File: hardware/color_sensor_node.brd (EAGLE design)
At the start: 27.9 x 27.9 mm, 20 parts, among them Q1 20V/4.2A/52mΩ/1.4W, U1 ISL29125, U2 3.3V, U3 WS2811

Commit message: Update color_sensor_node.brd
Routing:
- net 5V: track 49.7 -> 48.9 mm
- net GND: vias 23 -> 22

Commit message: add version number
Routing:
- net SCL: track 28.6 -> 28.1 mm
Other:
- board text added: "v01"
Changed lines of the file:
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@@
 <vertex x="5.08" y="15.24"/>
 </polygon>
+<text x="0.381" y="8.382" size="1.778" layer="1" font="vector" ratio="15" rot="SR270">v01</text>
 </plain>
 <attributes>
@@
 <wire x1="14.69" y1="14.47" x2="15.24" y2="14.47" width="0.2032" layer="1"/>
 <wire x1="16.51" y1="7.62" x2="21.59" y2="2.54" width="0.2032" layer="1"/>
-<wire x1="21.59" y1="4.445" x2="21.59" y2="2.54" width="0.4064" layer="16"/>
-<wire x1="21.59" y1="4.445" x2="20.828" y2="5.207" width="0.4064" layer="16"/>
-<wire x1="20.828" y1="5.207" x2="14.097" y2="5.207" width="0.4064" layer="16"/>
+<wire x1="21.59" y1="3.556" x2="21.59" y2="2.54" width="0.4064" layer="16"/>
+<wire x1="21.59" y1="3.556" x2="19.939" y2="5.207" width="0.4064" layer="16"/>
+<wire x1="19.939" y1="5.207" x2="14.097" y2="5.207" width="0.4064" layer="16"/>
 <wire x1="14.097" y1="5.207" x2="11.43" y2="2.54" width="0.4064" layer="16"/>
 <wire x1="15.24" y1="14.47" x2="16.51" y2="13.2" width="0.2032" layer="1"/>
@@
 <mfgpreviewcolor name="substratecolor" color="0xFF786E46"/>
 </mfgpreviewcolors>
-<errors>
-</errors>
 </board>
 </drawing>

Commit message: update packages, add rc filter to sensor vdd, move to smd connectors
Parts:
- removed J3: (no value), SparkFun-Connectors:2X5_PTH_SILK_.05
- added C3: 0.1uF, SparkFun-Capacitors:0603
- added J1: JTAG, SparkFun-Connectors:2X5-SMD-1.27MM
- added R3: 330, SparkFun-Resistors:0603
- D1: value WS2812-2020 -> WS2812B; device SparkFun-LED:WS2812-2020 -> SparkFun-LED:WS2812B
- J2: value (none) -> JTAG; device SparkFun-Connectors:2X5_PTH_SILK_.05 -> SparkFun-Connectors:2X5-SMD-1.27MM
- U3: device ws2811:MSOP8 -> ws2811:SOIC-8
- moved J2 12.8 mm to (19.1, 2.54)
- moved U1 5.08 mm to (19.1, 14.0)
- moved R1 3.54 mm to (17.8, 19.1), turned to 270 degrees
- moved D1 2.54 mm to (14.0, 14.0), turned to 180 degrees
- moved C1 1.27 mm to (8.13, 19.1)
- moved C2 1.27 mm to (2.54, 19.1)
- moved Q1 1.27 mm to (12.1, 19.1)
- moved R2 1.27 mm to (9.65, 19.1)
- moved U2 1.27 mm to (5.33, 19.1)
- moved U3 0.38 mm to (5.08, 14.0)
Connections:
- new net N$5: Q1.3, R3.2
- net 5V: now also D1.1, J1.4, J1.5, J1.7, J1.9; no longer D1.4, J3.4, J3.5, J3.7, J3.9
- net DIN: now also J1.6; no longer J2.6
- net DOUT: now also D1.2, J2.6; no longer D1.1, J3.6
- net GND: now also C3.2, D1.3, J1.1, J1.2, J1.3; no longer D1.2, J3.1, J3.2, J3.3
- net N$2: now also C3.1, R3.1; no longer Q1.3
- net N$4: now also D1.4; no longer D1.3
- net SCL: now also J1.10; no longer J3.10
- net SDA: now also J1.8; no longer J3.8
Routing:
- net 5V: track 48.9 -> 60.2 mm, vias 1 -> 0
- net GND: track 5.48 -> 16.5 mm, vias 22 -> 27
- net SCL: track 28.1 -> 36.5 mm
- net N$4: track 6.18 -> 10.7 mm
- net N$1: track 3.64 -> 7.65 mm
- net DIN: track 13.5 -> 16.2 mm
- net N$5: track 0.00 -> 2.43 mm
- net N$2: track 5.39 -> 7.02 mm
- net N$3: track 13.2 -> 14.1 mm
- net SDA: track 27.4 -> 26.6 mm, vias 2 -> 1

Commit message: Update color_sensor_node.brd
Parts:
- moved J1 12.5 mm to (3.81, 14.0), flipped to the bottom, turned to 90 degrees
- moved J2 12.5 mm to (24.1, 14.0), flipped to the bottom, turned to 90 degrees
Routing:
- net 5V: track 60.2 -> 28.5 mm, vias 0 -> 1
- net SCL: track 36.5 -> 11.1 mm, vias 0 -> 1
- net SDA: track 26.6 -> 8.64 mm
- net DOUT: track 14.3 -> 1.54 mm, vias 0 -> 1
- net DIN: track 16.2 -> 11.7 mm, vias 0 -> 1
- net GND: vias 27 -> 23

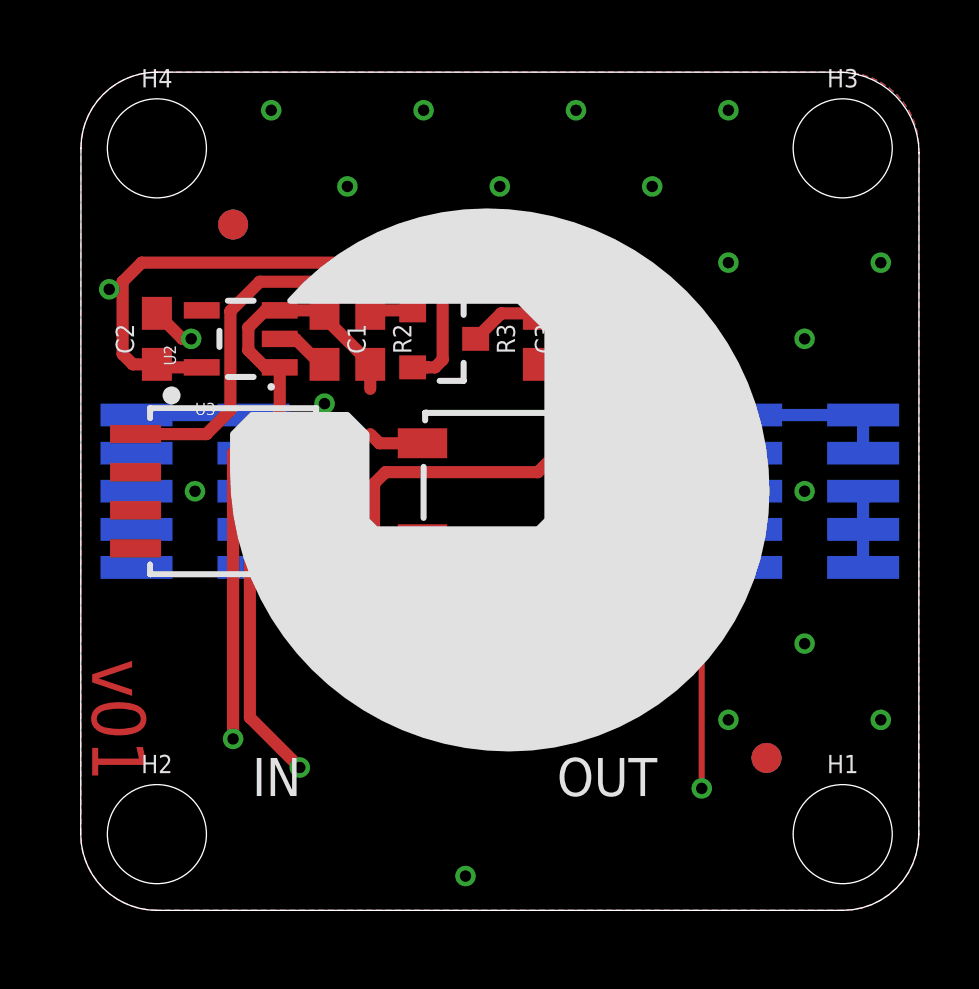
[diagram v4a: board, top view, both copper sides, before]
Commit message: simplify, remove mosfet
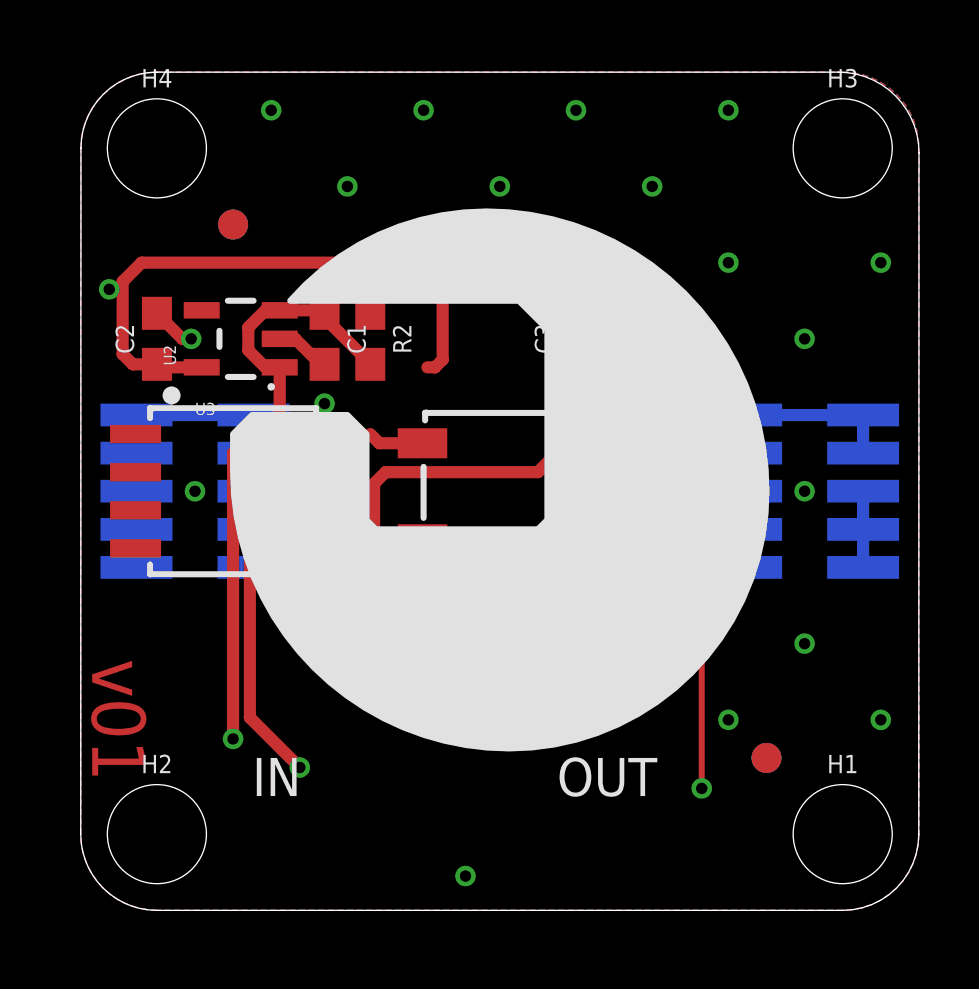
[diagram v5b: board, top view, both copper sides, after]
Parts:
- removed Q1: 20V/4.2A/52mΩ/1.4W, SparkFun-DiscreteSemi:SOT23-3
- removed R3: 330, SparkFun-Resistors:0603
- C3: value 0.1uF -> 1.0uF
- R2: value 287 -> 220
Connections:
- removed net N$3: Q1.1, R2.1, U3.1
- removed net N$5: Q1.3, R3.2
- net 3.3V: now also R2.2; no longer Q1.2
- net 5V: no longer R2.2
- net N$2: now also R2.1, U3.1; no longer R3.1
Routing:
- net N$3: track 14.1 -> 0.00 mm
- net N$5: track 2.43 -> 0.00 mm
- net N$2: track 7.02 -> 5.75 mm
- net 5V: track 28.5 -> 27.7 mm
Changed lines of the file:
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@@
 <attribute name="REV" value="" x="74.93" y="-20.32" size="1.778" layer="27" display="off"/>
-</element>
-<element name="Q1" library="SparkFun-DiscreteSemi" package="SOT23-3" value="20V/4.2A/52mΩ/1.4W" x="12.065" y="19.05" rot="R270">
-<attribute name="NAME" x="12.065" y="20.701" size="0.6096" layer="25" font="vector" ratio="20" align="bottom-center"/>
-<attribute name="PROD_ID" value="TRAN-14388" x="6.985" y="3.81" size="1.778" layer="27" rot="R270" display="off"/>
-<attribute name="VALUE" x="12.065" y="17.399" size="0.6096" layer="27" font="vector" ratio="20" align="top-center"/>
 </element>
 <element name="R1" library="SparkFun-Resistors" package="0603" value="10k" x="17.78" y="19.05" rot="R270">
@@
 <attribute name="VALUE" x="17.018" y="19.05" size="0.6096" layer="27" font="vector" ratio="20" rot="R270" align="top-center"/>
 </element>
-<element name="R2" library="SparkFun-Resistors" package="0603" value="287" x="9.652" y="19.05" rot="R270">
+<element name="R2" library="SparkFun-Resistors" package="0603" value="220" x="9.652" y="19.05" rot="R270">
 <attribute name="NAME" x="10.414" y="19.05" size="0.6096" layer="25" font="vector" ratio="20" rot="R270" align="bottom-center"/>
-<attribute name="PROD_ID" value="RES-10752" x="-18.288" y="-7.62" size="1.778" layer="27" rot="R270" display="off"/>
-<attribute name="VALUE" x="8.89" y="19.05" size="0.6096" layer="27" font="vector" ratio="20" rot="R270" align="top-center"/>
+<attribute name="PROD_ID" value="RES-07861" x="-18.288" y="-7.62" size="1.778" layer="27" rot="R270" display="off"/>
+<attribute name="VALUE" value="220" x="8.89" y="19.05" size="0.6096" layer="27" font="vector" ratio="20" rot="R270" align="top-center"/>
 </element>
 <element name="U1" library="SparkFun-Sensors" package="ODFN-6" value="ISL29125" x="19.05" y="13.97">
@@
 <attribute name="VALUE" value="JTAG" x="21.6662" y="12.1412" size="0.6096" layer="28" font="vector" ratio="20" rot="MR90"/>
 </element>
-<element name="C3" library="SparkFun-Capacitors" package="0603" value="0.1uF" x="16.51" y="19.05" rot="R90">
+<element name="C3" library="SparkFun-Capacitors" package="0603" value="1.0uF" x="16.51" y="19.05" rot="R90">
 <attribute name="NAME" x="15.748" y="19.05" size="0.6096" layer="25" font="vector" ratio="20" rot="R90" align="bottom-center"/>
-<attribute name="PROD_ID" value="CAP-00810" x="16.51" y="19.05" size="1.778" layer="27" font="vector" ratio="15" rot="R90" display="off"/>
-<attribute name="VALUE" value="0.1uF" x="17.272" y="19.05" size="0.6096" layer="27" font="vector" ratio="20" rot="R90" align="top-center"/>
-</element>
-<element name="R3" library="SparkFun-Resistors" package="0603" value="330" x="15.24" y="19.05" rot="R90">
-<attribute name="NAME" x="14.478" y="19.05" size="0.6096" layer="25" font="vector" ratio="20" rot="R90" align="bottom-center"/>
-<attribute name="PROD_ID" value="RES-00818" x="15.24" y="19.05" size="1.778" layer="27" font="vector" ratio="15" rot="R90" display="off"/>
-<attribute name="VALUE" value="330" x="16.002" y="19.05" size="0.6096" layer="27" font="vector" ratio="20" rot="R90" align="top-center"/>
+<attribute name="PROD_ID" value="CAP-00868" x="16.51" y="19.05" size="1.778" layer="27" font="vector" ratio="15" rot="R90" display="off"/>
+<attribute name="VALUE" value="1.0uF" x="17.272" y="19.05" size="0.6096" layer="27" font="vector" ratio="20" rot="R90" align="top-center"/>
 </element>
 </elements>
@@
 <contactref element="U2" pad="5"/>
 <contactref element="C2" pad="1"/>
-<contactref element="Q1" pad="2"/>
 <wire x1="4.0339" y1="18.1" x2="2.64" y2="18.1" width="0.4064" layer="1"/>
 <wire x1="2.64" y1="18.1" x2="2.54" y2="18.2" width="0.4064" layer="1"/>
-<wire x1="11.065" y1="18.1" x2="11.557" y2="18.1" width="0.4064" layer="1"/>
 <wire x1="11.557" y1="18.1" x2="11.811" y2="18.1" width="0.4064" layer="1"/>
 <wire x1="2.54" y1="18.2" x2="1.739" y2="18.2" width="0.4064" layer="1"/>
@@
 <wire x1="11.811" y1="18.1" x2="12.065" y2="18.354" width="0.4064" layer="1"/>
 <wire x1="12.065" y1="18.354" x2="12.065" y2="21.082" width="0.4064" layer="1"/>
+<contactref element="R2" pad="2"/>
+<wire x1="11.557" y1="18.1" x2="9.652" y2="18.2" width="0" layer="19" extent="1-1"/>
 </signal>
 <signal name="5V">
@@
 <contactref element="C1" pad="1"/>
 <contactref element="D1" pad="1"/>
-<contactref element="R2" pad="2"/>
 <wire x1="8.028" y1="20" x2="6.6341" y2="20" width="0.4064" layer="1"/>
 <wire x1="8.128" y1="19.9" x2="8.028" y2="20" width="0.4064" layer="1"/>
@@
 <wire x1="8.128" y1="19.9" x2="8.128" y2="19.75289375" width="0.4064" layer="1"/>
 <wire x1="9.652" y1="18.22889375" x2="8.128" y2="19.75289375" width="0.4064" layer="1"/>
-<wire x1="9.652" y1="18.22889375" x2="9.652" y2="18.2" width="0.4064" layer="1"/>
-<wire x1="9.652" y1="18.2" x2="9.652" y2="17.383" width="0.4064" layer="1"/>
 <contactref element="J1" pad="5"/>
 <contactref element="J1" pad="7"/>
@@
 <via x="5.08" y="5.715" extent="1-16" drill="0.381"/>
 <wire x1="26.08" y1="13.97" x2="22.18" y2="15.24" width="0" layer="19" extent="16-16"/>
-<wire x1="1.86" y1="15.24" x2="26.08" y2="11.43" width="0" layer="19" extent="16-16"/>
-<wire x1="5.76" y1="13.97" x2="1.86" y2="15.24" width="0" layer="19" extent="16-16"/>
-<wire x1="5.08" y1="5.715" x2="1.86" y2="15.24" width="0" layer="19" extent="1-16"/>
-<wire x1="9.652" y1="15.875" x2="9.652" y2="17.383" width="0" layer="19" extent="1-1"/>
+<wire x1="11.393" y1="15.57" x2="22.18" y2="15.24" width="0" layer="19" extent="1-16"/>
 <wire x1="8.3312" y1="15.875" x2="9.652" y2="15.875" width="0" layer="19" extent="1-1"/>
+<wire x1="6.6341" y1="15.9051" x2="8.3312" y2="15.875" width="0" layer="19" extent="1-1"/>
+<wire x1="5.76" y1="13.97" x2="5.08" y2="15.24" width="0" layer="19" extent="1-16"/>
+<wire x1="1.86" y1="15.24" x2="5.08" y2="15.24" width="0" layer="19" extent="1-16"/>
 </signal>
 <signal name="SDA">
@@
 <wire x1="11.393" y1="10.832" x2="22.18" y2="13.97" width="0" layer="19" extent="1-16"/>
 </signal>
-<signal name="N$2">
-<contactref element="R1" pad="2"/>
-<contactref element="U1" pad="1"/>
-<contactref element="R3" pad="1"/>
-<contactref element="C3" pad="1"/>
-<wire x1="15.24" y1="18.2" x2="16.51" y2="18.2" width="0.4064" layer="1"/>
-<wire x1="16.51" y1="18.2" x2="17.78" y2="18.2" width="0.4064" layer="1"/>
-<wire x1="18.405" y1="14.47" x2="18.661" y2="14.47" width="0.2032" layer="1"/>
-<wire x1="18.661" y1="14.47" x2="18.8214" y2="14.6304" width="0.2032" layer="1"/>
-<wire x1="18.8214" y1="17.1586" x2="17.78" y2="18.2" width="0.2032" layer="1"/>
-<wire x1="18.8214" y1="14.6304" x2="18.8214" y2="17.1586" width="0.2032" layer="1"/>
-</signal>
-<signal name="N$3">
-<contactref element="R2" pad="1"/>
-<contactref element="U3" pad="1"/>
-<contactref element="Q1" pad="1"/>
-<wire x1="11.065" y1="20" x2="9.752" y2="20" width="0.4064" layer="1"/>
-<wire x1="9.752" y1="20" x2="9.652" y2="19.9" width="0.4064" layer="1"/>
-<wire x1="4.9895" y1="19.9755" x2="4.9895" y2="16.6735" width="0.4064" layer="1"/>
-<wire x1="5.969" y1="20.955" x2="4.9895" y2="19.9755" width="0.4064" layer="1"/>
-<wire x1="9.271" y1="20.955" x2="5.969" y2="20.955" width="0.4064" layer="1"/>
-<wire x1="9.652" y1="20.574" x2="9.652" y2="19.9" width="0.4064" layer="1"/>
-<wire x1="9.652" y1="20.574" x2="9.271" y2="20.955" width="0.4064" layer="1"/>
-<wire x1="4.191" y1="15.875" x2="1.8288" y2="15.875" width="0.4064" layer="1"/>
-<wire x1="4.9895" y1="16.6735" x2="4.191" y2="15.875" width="0.4064" layer="1"/>
-</signal>
 <signal name="N$4">
 <contactref element="D1" pad="4"/>
@@
 <wire x1="16.205" y1="15.57" x2="15.24" y2="14.605" width="0.4064" layer="1"/>
 </signal>
-<signal name="N$5">
-<contactref element="Q1" pad="3"/>
-<contactref element="R3" pad="2"/>
-<wire x1="13.165" y1="19.05" x2="14.015" y2="19.9" width="0.4064" layer="1"/>
-<wire x1="14.015" y1="19.9" x2="15.24" y2="19.9" width="0.4064" layer="1"/>
+<signal name="N$2">
+<contactref element="U3" pad="1"/>
+<contactref element="R2" pad="1"/>
+<contactref element="R1" pad="2"/>
+<contactref element="U1" pad="1"/>
+<contactref element="C3" pad="1"/>
+<wire x1="16.51" y1="18.2" x2="17.78" y2="18.2" width="0.4064" layer="1"/>
+<wire x1="18.405" y1="14.47" x2="18.661" y2="14.47" width="0.2032" layer="1"/>
+<wire x1="18.661" y1="14.47" x2="18.8214" y2="14.6304" width="0.2032" layer="1"/>
+<wire x1="18.8214" y1="17.1586" x2="17.78" y2="18.2" width="0.2032" layer="1"/>
+<wire x1="18.8214" y1="14.6304" x2="18.8214" y2="17.1586" width="0.2032" layer="1"/>
+<wire x1="9.652" y1="19.9" x2="16.51" y2="18.2" width="0" layer="19" extent="1-1"/>
+<wire x1="1.8288" y1="15.875" x2="9.652" y2="19.9" width="0" layer="19" extent="1-1"/>
 </signal>
 </signals>
